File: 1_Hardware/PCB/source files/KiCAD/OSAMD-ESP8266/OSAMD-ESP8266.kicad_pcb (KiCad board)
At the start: 2 copper layers, 85 x 70 mm, 21 parts, among them J1 DHT-Socket, J2 MQ-135 Conn, J3 LCD Conn, J6 USB_B, J7 Socket_D1_Mini_01_08, J8 Socket_D1_Mini_09_16, SW1 SW_Pushbutton, U1 LCD1

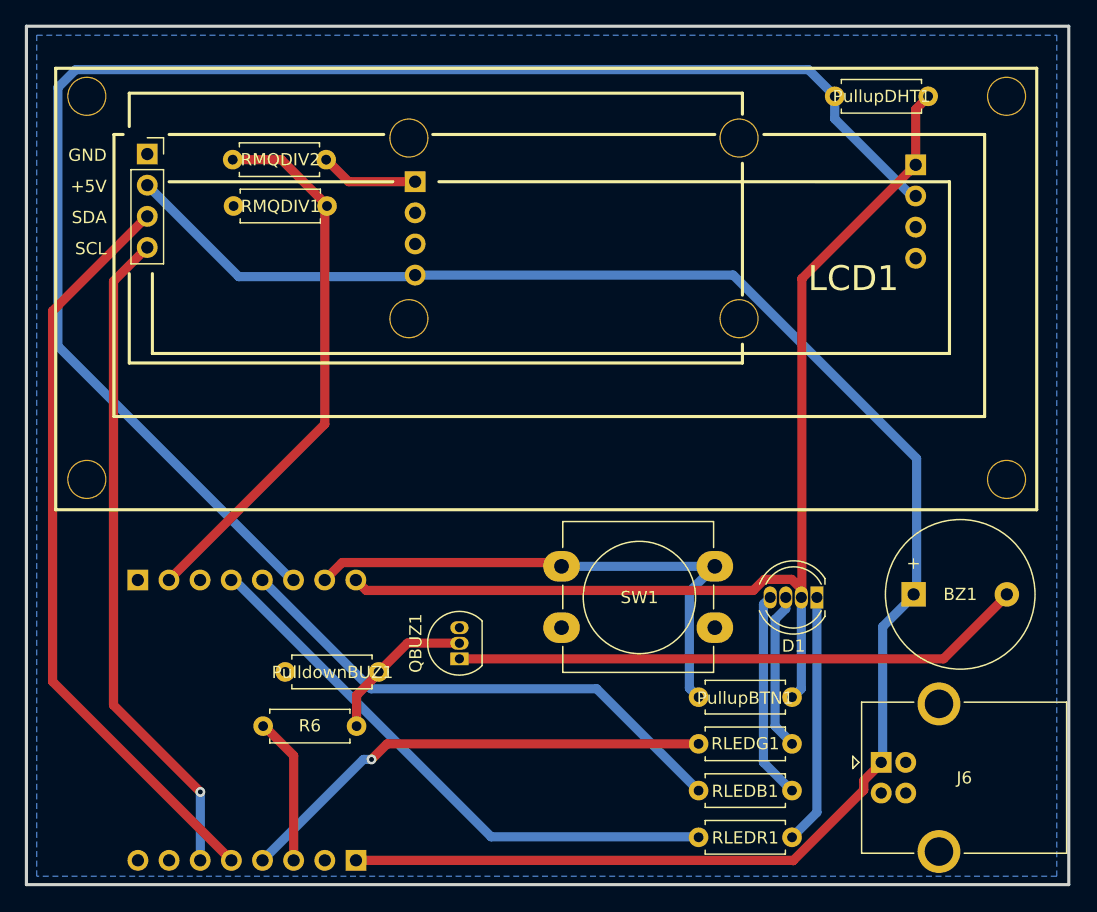
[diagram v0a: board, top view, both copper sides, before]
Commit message: switched button and buzzer pin
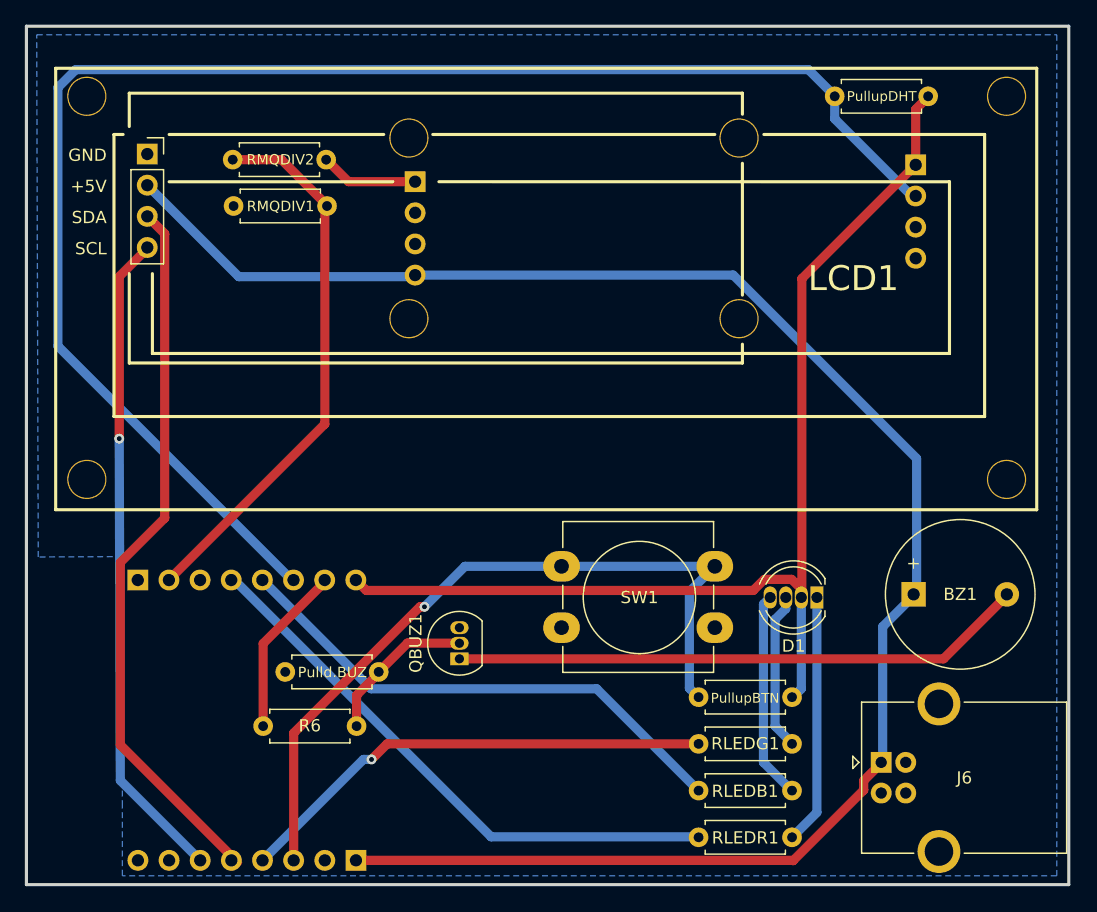
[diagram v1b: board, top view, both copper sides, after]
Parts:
- renumbered PulldownBUZ1 to Pulld.BUZ, PullupBTN1 to PullupBTN, PullupDHT1 to PullupDHT
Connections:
- J7 pad 7: /BTN -> /BUZZER
- J8 pad 3: /BUZZER -> /BTN
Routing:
- net /BTN: track 44.3 -> 62.2 mm, vias 0 -> 1
- net /LCD_SDA: track 61.8 -> 58.7 mm
- net /BUZZER: track 11.8 -> 13.8 mm
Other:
- board text added: "Antenna"

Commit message: rounded edges on the pcb set gerber settings for jlcpcb
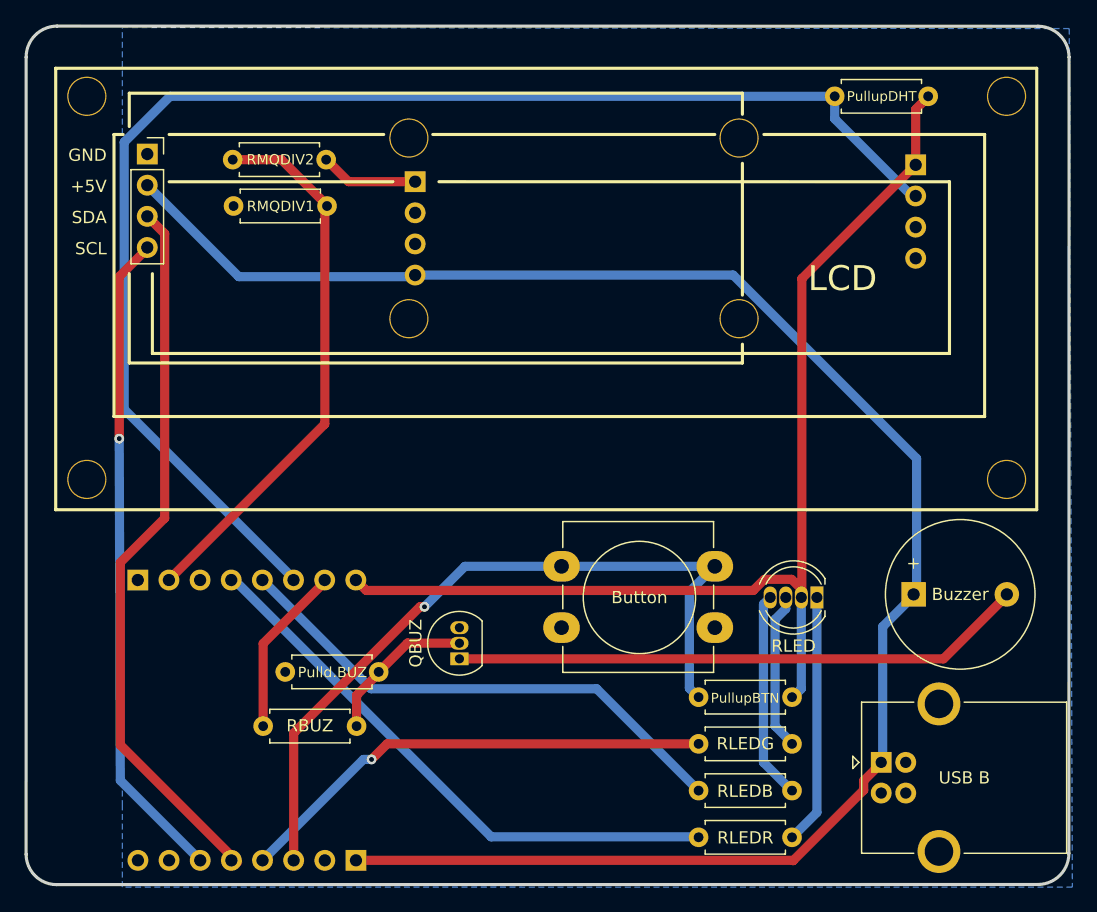
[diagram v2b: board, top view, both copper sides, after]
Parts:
- U1: value LCD1 -> LCD
- USB B: renamed from J6
- renumbered SW1 to Button, BZ1 to Buzzer, QBUZ1 to QBUZ, R6 to RBUZ, D1 to RLED, RLEDB1 to RLEDB, RLEDG1 to RLEDG, RLEDR1 to RLEDR
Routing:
- net /DHT Data: track 124.3 -> 112.0 mm
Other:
- board size 85 x 70 mm -> 85.1 x 70 mm
- board text added: "based on Open-Source Air Monitoring Device by Paul Goldschmidt in Heidelberg, Germany"
- board text removed: "Open-Source Air Monitoring Device"
- board text removed: "by Paul Goldschmidt in Heidelberg, Germany"
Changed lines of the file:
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@@
       (plot_on_all_layers_selection 0x0000000_00000000)
       (disableapertmacros false)
-      (usegerberextensions false)
+      (usegerberextensions true)
       (usegerberattributes true)
-      (usegerberadvancedattributes true)
-      (creategerberjobfile true)
+      (usegerberadvancedattributes false)
+      (creategerberjobfile false)
       (dashed_line_dash_ratio 12.000000)
       (dashed_line_gap_ratio 3.000000)
@@
       (psa4output false)
       (plotreference true)
-      (plotvalue true)
+      (plotvalue false)
       (plotinvisibletext false)
       (sketchpadsonfab false)
-      (subtractmaskfromsilk false)
+      (subtractmaskfromsilk true)
       (outputformat 1)
       (mirror false)
-      (drillshape 1)
+      (drillshape 0)
       (scaleselection 1)
-      (outputdirectory "")
+      (outputdirectory "OSAMD-ESP8266-gerber/")
     )
   )
@@
     (property "ki_keywords" "switch normally-open pushbutton push-button")
     (attr through_hole)
-    (fp_text reference "SW1" (at 6.35 2.54) (layer "F.SilkS")
+    (fp_text reference "Button" (at 6.35 2.54) (layer "F.SilkS")
         (effects (font (size 1 1) (thickness 0.15)))
     )
@@
     (property "ki_keywords" "connector USB")
     (attr through_hole)
-    (fp_text reference "J6" (at 6.7775 1.26) (layer "F.SilkS")
+    (fp_text reference "USB B" (at 6.7775 1.26) (layer "F.SilkS")
         (effects (font (size 1 1) (thickness 0.15)))
     )
@@
     (property "ki_keywords" "R res resistor")
     (attr through_hole)
-    (fp_text reference "RLEDR1" (at 3.81 0.04) (layer "F.SilkS")
+    (fp_text reference "RLEDR" (at 3.81 0.04) (layer "F.SilkS")
         (effects (font (size 1 1) (thickness 0.15)))
     )
@@
     (property "ki_keywords" "R res resistor")
     (attr through_hole)
-    (fp_text reference "RLEDB1" (at 3.79 0.05) (layer "F.SilkS")
+    (fp_text reference "RLEDB" (at 3.79 0.05) (layer "F.SilkS")
         (effects (font (size 1 1) (thickness 0.15)))
     )
@@
     (property "ki_keywords" "R res resistor")
     (attr through_hole)
-    (fp_text reference "R6" (at 3.81 -0.0322) (layer "F.SilkS")
+    (fp_text reference "RBUZ" (at 3.81 -0.0322) (layer "F.SilkS")
         (effects (font (size 1 1) (thickness 0.15)))
     )
@@
     (property "ki_keywords" "quartz resonator ceramic")
     (attr through_hole)
-    (fp_text reference "BZ1" (at 3.8 0) (layer "F.SilkS")
+    (fp_text reference "Buzzer" (at 3.8 0) (layer "F.SilkS")
         (effects (font (size 1 1) (thickness 0.15)))
     )
@@
         (effects (font (size 1.143 1.143) (thickness 0.152)) (justify left))
     )
-    (fp_text value "LCD1" (at 61.341 17.145) (layer "F.SilkS")
+    (fp_text value "LCD" (at 61.341 17.145) (layer "F.SilkS")
         (effects (font (size 2.032 2.032) (thickness 0.203)) (justify left))
     )
@@
     (property "ki_keywords" "R res resistor")
     (attr through_hole)
-    (fp_text reference "RLEDG1" (at 3.81 -0.02) (layer "F.SilkS")
+    (fp_text reference "RLEDG" (at 3.81 -0.02) (layer "F.SilkS")
         (effects (font (size 1 1) (thickness 0.15)))
     )
@@
     (property "ki_keywords" "LED RGB diode")
     (attr through_hole)
-    (fp_text reference "D1" (at 1.905 -3.96) (layer "F.SilkS")
+    (fp_text reference "RLED" (at 1.905 -3.96) (layer "F.SilkS")
         (effects (font (size 1 1) (thickness 0.15)))
     )
@@
     (property "ki_keywords" "NPN Transistor")
     (attr through_hole)
-    (fp_text reference "QBUZ1" (at 1.27 -3.56 90) (layer "F.SilkS")
+    (fp_text reference "QBUZ" (at 1.27 -3.56 90) (layer "F.SilkS")
         (effects (font (size 1 1) (thickness 0.15)))
     )
@@
     )
   )
-  (gr_line (start 172.427 63.3985) (end 172.427 133.3985)
+  (gr_line (start 172.451889 65.921433) (end 172.438361 130.846763)
     (stroke (width 0.254) (type solid)) (layer "Edge.Cuts"))
-  (gr_line (start 87.427 63.3985) (end 172.427 63.3985)
+  (gr_arc (start 169.911963 63.400639) (mid 171.704 64.135) (end 172.451889 65.921433)
+    (stroke (width 0.254) (type default)) (layer "Edge.Cuts"))
+  (gr_arc (start 87.403639 65.927037) (mid 88.138 64.135) (end 89.924433 63.387111)
+    (stroke (width 0.254) (type default)) (layer "Edge.Cuts"))
+  (gr_arc (start 172.438361 130.846763) (mid 171.704 132.6388) (end 169.917567 133.386689)
+    (stroke (width 0.254) (type default)) (layer "Edge.Cuts"))
+  (gr_line (start 89.924433 63.387111) (end 169.911963 63.400639)
     (stroke (width 0.254) (type solid)) (layer "Edge.Cuts"))
-  (gr_line (start 87.427 133.3985) (end 87.427 63.3985)
+  (gr_line (start 87.4 130.928567) (end 87.403639 65.927037)
     (stroke (width 0.254) (type solid)) (layer "Edge.Cuts"))
-  (gr_line (start 172.427 133.3985) (end 87.427 133.3985)
+  (gr_arc (start 89.894475 133.399) (mid 88.138042 132.679383) (end 87.4 130.928567)
+    (stroke (width 0.254) (type default)) (layer "Edge.Cuts"))
+  (gr_line (start 169.917567 133.386689) (end 89.894475 133.399)
     (stroke (width 0.254) (type solid)) (layer "Edge.Cuts"))
   (gr_rect locked (start 146.74 106.73) (end 153.24 113.23)
@@
     (effects (font (size 1 1) (thickness 0.15)) (justify left bottom mirror))
   )
-  (gr_text "Open-Source Air Monitoring Device" (at 157.1498 101.7016) (layer "B.SilkS")
+  (gr_text "based on\nOpen-Source Air Monitoring Device\nby Paul Goldschmidt in Heidelberg, Germany" (at 164.084 98.298) (layer "B.SilkS")
     (effects (font (size 2 2) (thickness 0.152)) (justify left mirror))
   )
@@
     (effects (font (size 1 1) (thickness 0.15)) (justify right mirror))
   )
-  (gr_text "by Paul Goldschmidt in Heidelberg, Germany" (at 163.3318 98.6536) (layer "B.SilkS")
-    (effects (font (size 2 2) (thickness 0.152)) (justify left mirror))
-  )
   (gr_text "5V" (at 114.3 129.54 90) (layer "B.SilkS")
     (effects (font (size 1 1) (thickness 0.15)) (justify right mirror))
@@
     (effects (font (size 1 1) (thickness 0.15)) (justify right))
   )
-  (segment (start 151.1984 66.9384) (end 153.4 69.14) (width 0.75) (layer "B.Cu") (net 1))
   (segment (start 153.34 69.1135) (end 153.34 70.9475) (width 0.75) (layer "B.Cu") (net 1))
-  (segment (start 89.9942 89.4842) (end 109.17 108.66) (width 0.75) (layer "B.Cu") (net 1))
-  (segment (start 89.9942 68.397685) (end 91.453485 66.9384) (width 0.75) (layer "B.Cu") (net 1))
+  (segment (start 99.1409 69.1135) (end 95.399859 72.854541) (width 0.75) (layer "B.Cu") (net 1))
+  (segment (start 95.399859 94.637859) (end 109.22 108.458) (width 0.75) (layer "B.Cu") (net 1))
   (segment (start 153.34 70.9475) (end 159.6625 77.27) (width 0.75) (layer "B.Cu") (net 1))
-  (segment (start 89.9942 68.397685) (end 89.9942 89.4842) (width 0.75) (layer "B.Cu") (net 1))
+  (segment (start 95.399859 72.854541) (end 95.399859 94.637859) (width 0.75) (layer "B.Cu") (net 1))
   (segment (start 159.6625 77.27) (end 160.02 77.27) (width 0.75) (layer "B.Cu") (net 1))
-  (segment (start 91.453485 66.9384) (end 151.1984 66.9384) (width 0.75) (layer "B.Cu") (net 1))
+  (segment (start 153.34 69.1135) (end 99.1409 69.1135) (width 0.75) (layer "B.Cu") (net 1))
   (segment (start 125.323144 129.5) (end 142.27 129.5) (width 0.75) (layer "B.Cu") (net 2))
   (segment (start 104.1296 108.5592) (end 104.382344 108.5592) (width 0.75) (layer "B.Cu") (net 2))
@@
     (polygon
       (pts
-        (xy 171.45 132.675586)
-        (xy 95.25 132.675586)
+        (xy 172.72 133.604)
+        (xy 95.25 133.604)
         (xy 95.25 127)
         (xy 95.25 106.648888)
-        (xy 88.392 106.68)
-        (xy 88.265 64.095586)
-        (xy 171.45 64.095586)
+        (xy 95.25 63.5)
+        (xy 172.466 63.587586)
       )
     )
